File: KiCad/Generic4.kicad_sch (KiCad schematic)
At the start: 11 parts, among them J1 I/O, J2 SPOX, U1 ESP32-PICO-MINI-02, U2 LMR16006+FB

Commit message: Tidy
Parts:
- added D1: RGB, RevK:LED-RGB-1.6x1.6, symbol Device:LED_ARGB
- added R1: 680R, RevK:R_0603, symbol Device:R
- added R2: 2K, RevK:R_0603, symbol Device:R
- added R3: 220R, RevK:R_0603, symbol Device:R
- renumbered D1 to D2, R1 to R4, R2 to R5
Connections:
- net +3V3: now also D1.1 (A)
- net R: now reaches U1.33 (IO19)
- net R: now also R1.2
- net G: now reaches U1.34 (IO22)
- net G: now also R2.2
- new net: D1.2 (RK), R1.1
- new net: D1.3 (GK), R2.1
- new net: D1.4 (BK), R3.1
- new net B: R3.2
- no-connect marks 17 -> 14

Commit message: Tweak
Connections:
- net B: now also U1.26 (IO20)
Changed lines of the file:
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@@
     )
   )
-  (global_label "B" (shape input) (at 43.18 73.66 0) (fields_autoplaced)
+  (global_label "B" (shape input) (at 81.28 66.04 0) (fields_autoplaced)
     (effects (font (size 1.27 1.27)) (justify left))
-    (property "Intersheet References" "${INTERSHEET_REFS}" (id 0) (at 146.05 179.07 0)
+    (property "Intersheet References" "${INTERSHEET_REFS}" (id 0) (at 184.15 171.45 0)
       (effects (font (size 1.27 1.27)) hide)
     )

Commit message: Started on Generic5
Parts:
- J1: footprint Connector_PinHeader_2.54mm:PinHeader_2x04_P2.54mm_Vertical -> Connector_PinHeader_2.54mm:PinHeader_2x05_P2.54mm_Vertical; symbol Connector_Generic:Conn_02x04_Top_Bottom -> Connector_Generic:Conn_02x05_Odd_Even; now in the parts list
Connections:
- net +3V3: now also J1.5 (Pin_5)
- net B: now also U1.27 (IO7); no longer U1.26 (IO20)
- net G: now also U1.33 (IO19); no longer U1.34 (IO22)
- net GND: now also J1.1 (Pin_1)
- net GPIO0: now also J1.3 (Pin_3); no longer J1.1 (Pin_1)
- net IO2: now also J1.4 (Pin_4); no longer J1.3 (Pin_3)
- net IO3: now also J1.6 (Pin_6); no longer J1.4 (Pin_4)
- net IO4: now also J1.8 (Pin_8); no longer J1.5 (Pin_5)
- net IO5: now also J1.10 (Pin_10), U1.26 (IO20); no longer J1.6 (Pin_6), U1.20 (IO13)
- net IO6: now also J2.3 (Pin_3); no longer J1.7 (Pin_7)
- net IO7: now also J2.4 (Pin_4); no longer J1.8 (Pin_8)
- net R: now also U1.34 (IO22); no longer U1.33 (IO19)
- net RX: now also J1.7 (Pin_7); no longer J2.4 (Pin_4)
- net TX: now also J1.9 (Pin_9); no longer J2.3 (Pin_3)
- no-connect marks 14 -> 12

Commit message: Ready for order
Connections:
- no-connect marks 12 -> 14
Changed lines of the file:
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@@
   (junction (at 136.525 43.18) (diameter 0) (color 0 0 0 0)
   )
+  (no_connect (at 50.8 76.2))
+  (no_connect (at 50.8 81.28))
   (no_connect (at 50.8 45.72))
   (no_connect (at 50.8 48.26))

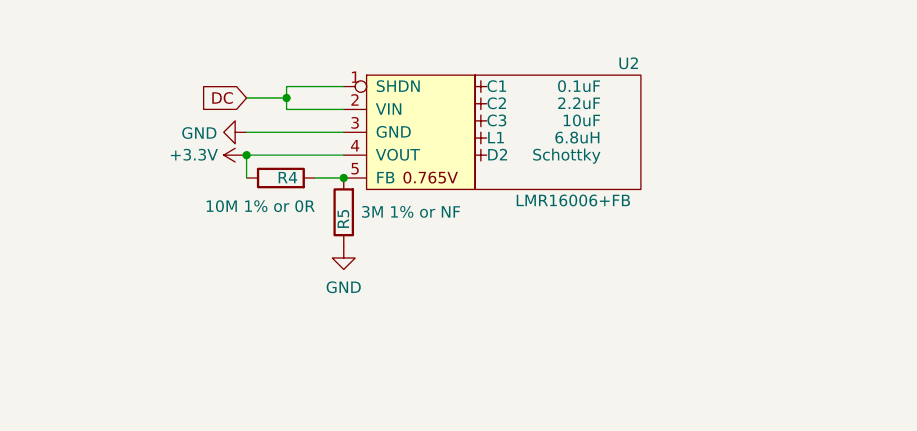
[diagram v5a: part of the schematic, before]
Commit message: Tweak for smoother power, and change of regulator FB pot divide
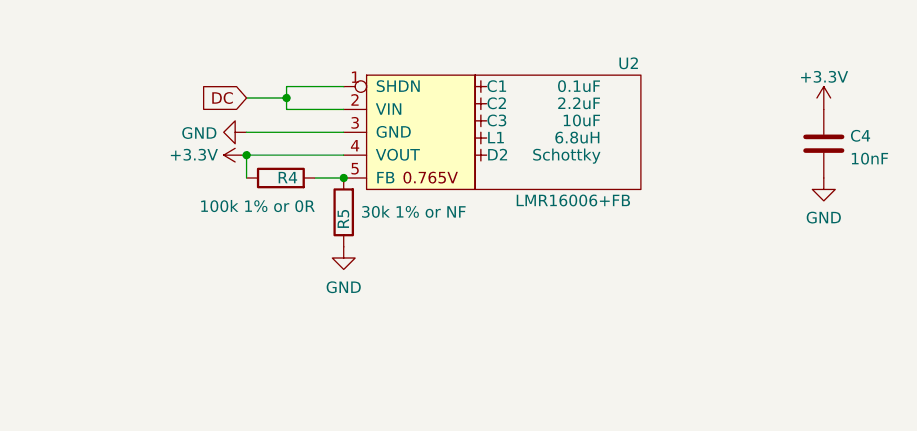
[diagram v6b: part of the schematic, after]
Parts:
- added C4: 10nF, RevK:C_0603, symbol Device:C
- R4: value 10M 1% or 0R -> 100k 1% or 0R
- R5: value 3M 1% or NF -> 30k 1% or NF
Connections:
- net +3V3: now also C4.1
- net GND: now also C4.2
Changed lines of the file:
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@@
   (symbol (lib_id "power:GND") (at 142.24 81.28 270) (unit 1)
     (in_bom yes) (on_board yes) (fields_autoplaced)
-    (property "Reference" "#PWR06" (id 0) (at 135.89 81.28 0)
+    (property "Reference" "#PWR08" (id 0) (at 135.89 81.28 0)
       (effects (font (size 1.27 1.27)) hide)
     )
@@
     (pin "1")
   )
+  (symbol (lib_id "Device:C") (at 200.66 41.91 0) (unit 1)
+    (in_bom yes) (on_board yes) (fields_autoplaced)
+    (property "Reference" "C4" (id 0) (at 203.581 41.0753 0)
+      (effects (font (size 1.27 1.27)) (justify left))
+    )
+    (property "Value" "10nF" (id 1) (at 203.581 43.6122 0)
+      (effects (font (size 0 0)) (justify left))
+    )
+    (property "Footprint" "RevK:C_0603" (id 2) (at 201.6252 45.72 0)
+      (effects (font (size 1.27 1.27)) hide)
+    )
+    (property "Datasheet" "~" (id 3) (at 200.66 41.91 0)
+      (effects (font (size 1.27 1.27)) hide)
+    )
+    (pin "1")
+    (pin "2")
+  )
   (symbol (lib_id "power:+3.3V") (at 71.12 116.84 270) (unit 1)
     (in_bom yes) (on_board yes)
@@
   (symbol (lib_id "power:GND") (at 147.32 53.34 0) (unit 1)
     (in_bom yes) (on_board yes) (fields_autoplaced)
-    (property "Reference" "#PWR07" (id 0) (at 147.32 59.69 0)
+    (property "Reference" "#PWR09" (id 0) (at 147.32 59.69 0)
       (effects (font (size 1.27 1.27)) hide)
     )
@@
       (effects (font (size 1.27 1.27)) (justify right))
     )
-    (property "Value" "3M 1% or NF" (id 1) (at 149.225 49.53 0)
+    (property "Value" "30k 1% or NF" (id 1) (at 149.225 49.53 0)
       (effects (font (size 1.27 1.27)) (justify right))
     )
@@
   (symbol (lib_id "power:GND") (at 139.7 99.06 270) (unit 1)
     (in_bom yes) (on_board yes)
-    (property "Reference" "#PWR0102" (id 0) (at 133.35 99.06 0)
+    (property "Reference" "#PWR06" (id 0) (at 133.35 99.06 0)
       (effects (font (size 1.27 1.27)) hide)
     )
@@
   (symbol (lib_id "power:+3.3V") (at 139.7 104.14 90) (unit 1)
     (in_bom yes) (on_board yes) (fields_autoplaced)
-    (property "Reference" "#PWR0101" (id 0) (at 143.51 104.14 0)
+    (property "Reference" "#PWR07" (id 0) (at 143.51 104.14 0)
       (effects (font (size 1.27 1.27)) hide)
     )
@@
     (pin "3")
     (pin "4")
+  )
+  (symbol (lib_id "power:+3.3V") (at 200.66 38.1 0) (unit 1)
+    (in_bom yes) (on_board yes) (fields_autoplaced)
+    (property "Reference" "#PWR010" (id 0) (at 200.66 41.91 0)
+      (effects (font (size 1.27 1.27)) hide)
+    )
+    (property "Value" "+3.3V" (id 1) (at 200.66 34.5242 0))
+    (property "Footprint" "" (id 2) (at 200.66 38.1 0)
+      (effects (font (size 1.27 1.27)) hide)
+    )
+    (property "Datasheet" "" (id 3) (at 200.66 38.1 0)
+      (effects (font (size 1.27 1.27)) hide)
+    )
+    (pin "1")
   )
   (symbol (lib_id "Device:LED_ARGB") (at 66.04 116.84 0) (unit 1)
@@
     (pin "2")
   )
+  (symbol (lib_id "power:GND") (at 200.66 45.72 0) (unit 1)
+    (in_bom yes) (on_board yes) (fields_autoplaced)
+    (property "Reference" "#PWR011" (id 0) (at 200.66 52.07 0)
+      (effects (font (size 1.27 1.27)) hide)
+    )
+    (property "Value" "GND" (id 1) (at 200.66 50.1634 0))
+    (property "Footprint" "" (id 2) (at 200.66 45.72 0)
+      (effects (font (size 1.27 1.27)) hide)
+    )
+    (property "Datasheet" "" (id 3) (at 200.66 45.72 0)
+      (effects (font (size 1.27 1.27)) hide)
+    )
+    (pin "1")
+  )
   (symbol (lib_id "Device:R") (at 140.335 45.72 90) (unit 1)
     (in_bom yes) (on_board yes)
@@
       (effects (font (size 1.27 1.27)) (justify left))
     )
-    (property "Value" "10M 1% or 0R" (id 1) (at 144.145 48.895 90)
+    (property "Value" "100k 1% or 0R" (id 1) (at 144.145 48.895 90)
       (effects (font (size 1.27 1.27)) (justify left))
     )
@@
       (reference "#PWR05") (unit 1) (value "+3.3V") (footprint "")
     )
+    (path "/9305e158-b3ff-460b-ad9b-735d807fea63"
+      (reference "#PWR06") (unit 1) (value "GND") (footprint "")
+    )
+    (path "/a5f1d1b0-d50c-4a68-ac30-c1da66e777f9"
+      (reference "#PWR07") (unit 1) (value "+3.3V") (footprint "")
+    )
     (path "/1e8ea742-99a3-47cc-bbc1-ed8989b74db8"
-      (reference "#PWR06") (unit 1) (value "GND") (footprint "")
+      (reference "#PWR08") (unit 1) (value "GND") (footprint "")
     )
     (path "/43ac1e5e-55b4-4274-a7ec-fd3947e95aec"
-      (reference "#PWR07") (unit 1) (value "GND") (footprint "")
-    )
-    (path "/a5f1d1b0-d50c-4a68-ac30-c1da66e777f9"
-      (reference "#PWR0101") (unit 1) (value "+3.3V") (footprint "")
-    )
-    (path "/9305e158-b3ff-460b-ad9b-735d807fea63"
-      (reference "#PWR0102") (unit 1) (value "GND") (footprint "")
+      (reference "#PWR09") (unit 1) (value "GND") (footprint "")
+    )
+    (path "/b8f1f158-9ded-4572-b813-5295c6b7e555"
+      (reference "#PWR010") (unit 1) (value "+3.3V") (footprint "")
+    )
+    (path "/f7a2cf2e-033d-4a1a-9ac8-18e3c1c37533"
+      (reference "#PWR011") (unit 1) (value "GND") (footprint "")
     )
     (path "/00000000-0000-0000-0000-0000610f9b88"
@@
       (reference "C3") (unit 1) (value "10uF") (footprint "RevK:Hidden")
     )
+    (path "/296b967f-b7a9-453f-856a-7b874fdca3db"
+      (reference "C4") (unit 1) (value "10nF") (footprint "RevK:C_0603")
+    )
     (path "/c402b2b8-0bbd-4038-b1b9-845d84949881"
       (reference "D1") (unit 1) (value "RGB") (footprint "RevK:LED-RGB-1.6x1.6")
@@
     )
     (path "/fc3ca677-79f2-42b6-a5b3-ff3b18df1d6c"
-      (reference "R4") (unit 1) (value "10M 1% or 0R") (footprint "RevK:R_0603")
+      (reference "R4") (unit 1) (value "100k 1% or 0R") (footprint "RevK:R_0603")
     )
     (path "/83151023-5106-4495-aeff-aefc75dfd6c0"
-      (reference "R5") (unit 1) (value "3M 1% or NF") (footprint "RevK:R_0603")
+      (reference "R5") (unit 1) (value "30k 1% or NF") (footprint "RevK:R_0603")
     )
     (path "/7943a3d5-b195-4a57-b3e1-ee29355f1eeb"

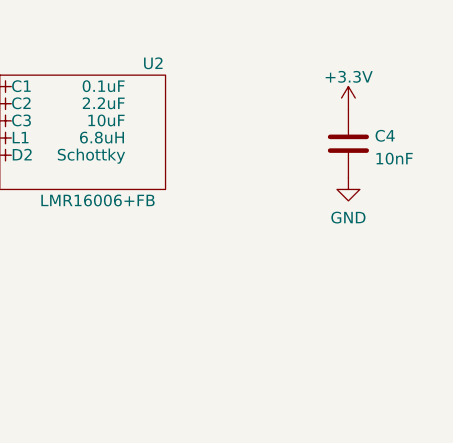
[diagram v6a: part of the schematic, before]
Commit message: Change resistor values
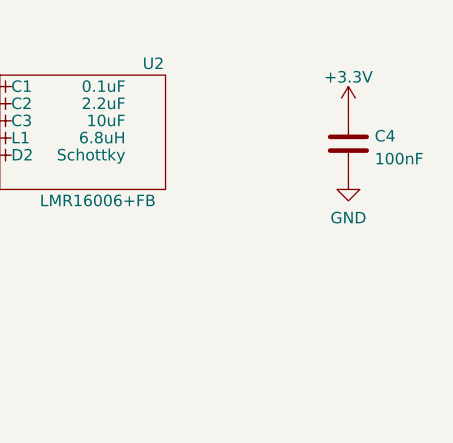
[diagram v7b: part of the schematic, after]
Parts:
- C4: value 10nF -> 100nF
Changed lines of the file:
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@@
       (effects (font (size 1.27 1.27)) (justify left))
     )
-    (property "Value" "10nF" (id 1) (at 203.581 43.6122 0)
-      (effects (font (size 0 0)) (justify left))
+    (property "Value" "100nF" (id 1) (at 203.581 43.6122 0)
+      (effects (font (size 1.27 1.27)) (justify left))
     )
     (property "Footprint" "RevK:C_0603" (id 2) (at 201.6252 45.72 0)
@@
     )
     (path "/296b967f-b7a9-453f-856a-7b874fdca3db"
-      (reference "C4") (unit 1) (value "10nF") (footprint "RevK:C_0603")
+      (reference "C4") (unit 1) (value "100nF") (footprint "RevK:C_0603")
     )
     (path "/c402b2b8-0bbd-4038-b1b9-845d84949881"

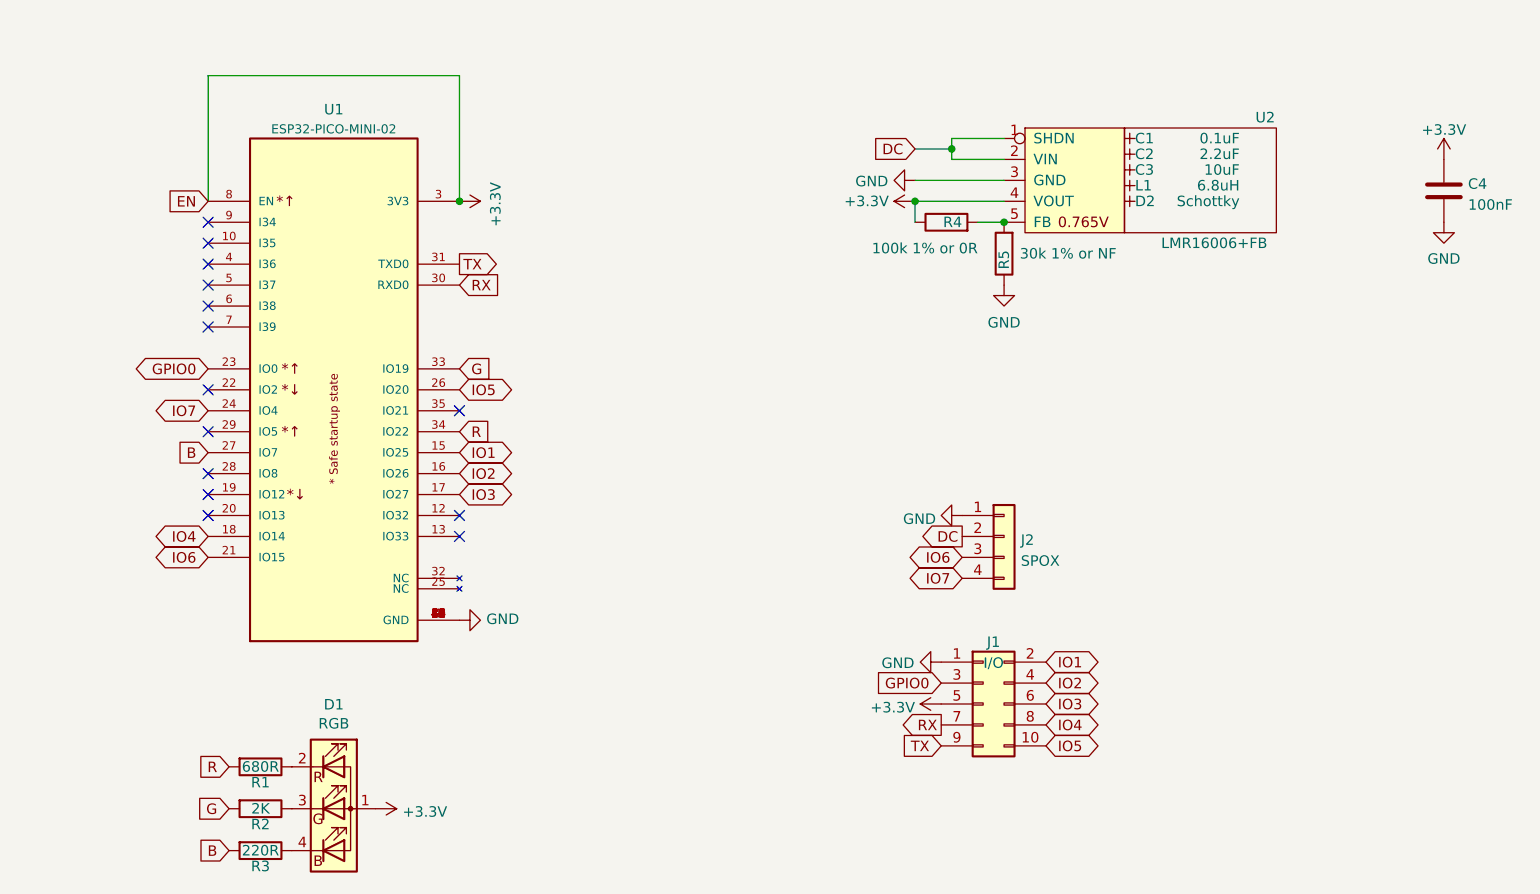
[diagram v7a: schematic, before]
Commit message: Changed to have C/R for EN
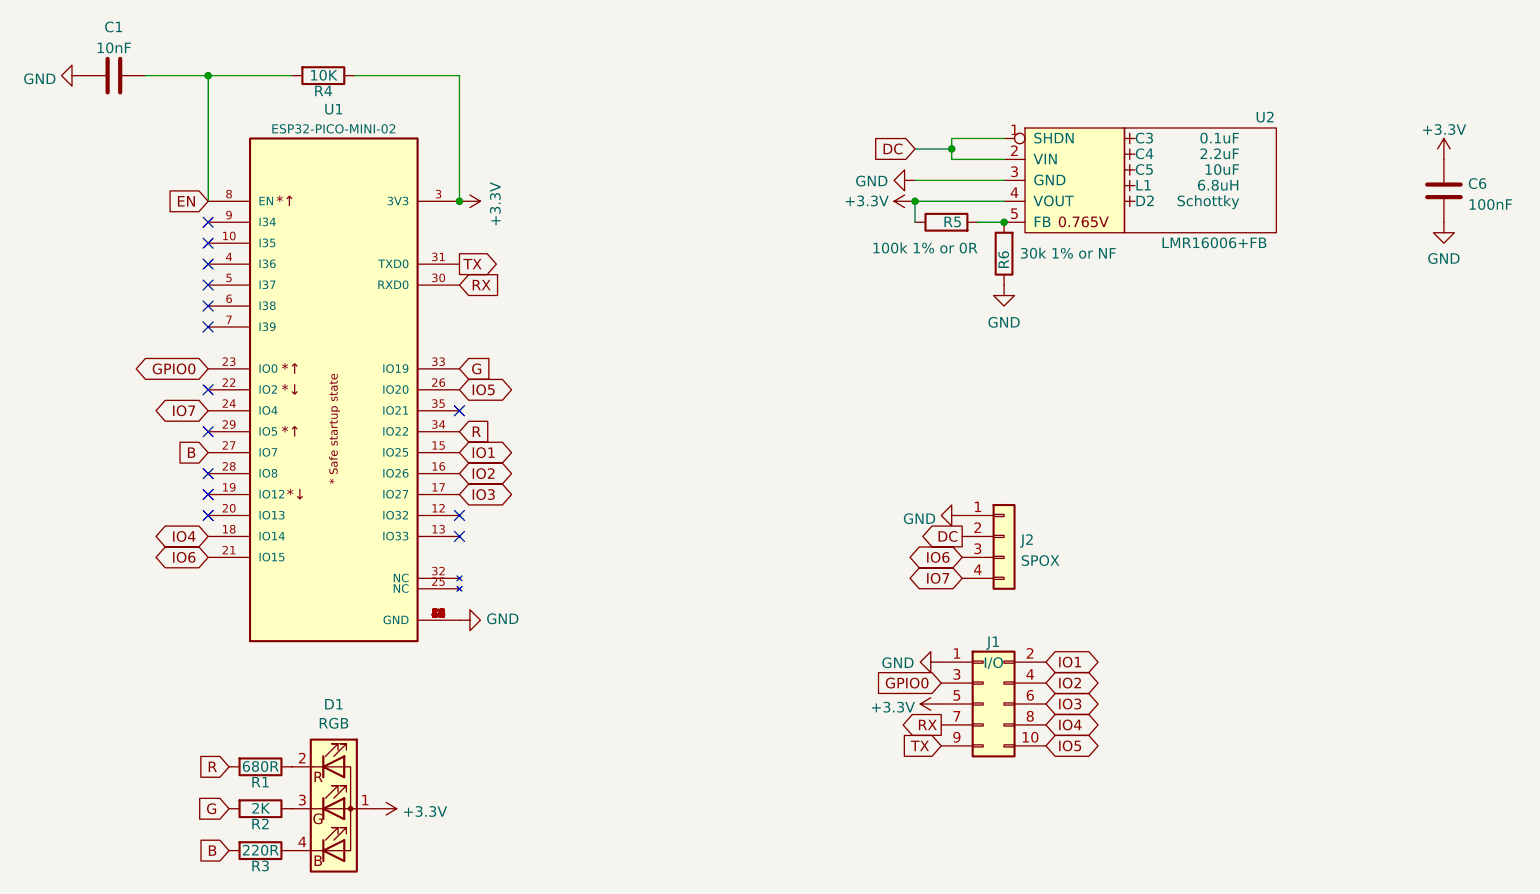
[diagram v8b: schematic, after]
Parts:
- added C1: 10nF, RevK:C_0603, symbol Device:C
- added R4: 10K, RevK:R_0603, symbol Device:R
- renumbered C1 to C3, C2 to C4, C3 to C5, C4 to C6, R4 to R5, R5 to R6
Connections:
- net +3V3: now also R4.1; no longer U1.8 (EN)
- net GND: now also C1.1
- new net EN: C1.2, R4.2, U1.8 (EN)
